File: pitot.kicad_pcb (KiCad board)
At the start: 2 copper layers, 15 parts, among them IC1 LT1167CN8PBF, IC2 LT1167CN8PBF, IC3 LT1167CN8PBF, IC4 LTC1144CN8#PBF, IC5 DEV-11114, P1 DIL8, P2 DIL8, P3 DIL8, P4 CONN_01X04, U1 LM7809CT

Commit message: size adj
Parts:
- moved P3 47.9 mm to (149.9, 53.3)
- moved P4 40.7 mm to (96.5, 96.5)
- moved P2 32.1 mm to (129.5, 53.3)
- moved IC5 30.5 mm to (109.2, 101.6)
- moved R3 28.1 mm to (157.5, 68.6)
- moved IC3 25.4 mm to (152.4, 68.6)
- moved P1 20.5 mm to (109.2, 53.3)
- moved R2 15.5 mm to (137.2, 68.6)
- moved IC2 12.7 mm to (132.1, 68.6)
- moved R1 3.59 mm to (116.8, 68.6)
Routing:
- net +5V: track 322.6 -> 170.2 mm
- net (no net): track 86.4 -> 0.00 mm
- net GND: track 457.0 -> 371.5 mm
- net Net-(IC5-Pad1): track 94.2 -> 33.9 mm
- net Net-(IC5-Pad2): track 87.9 -> 30.9 mm
- net Net-(IC3-Pad6): track 93.5 -> 40.6 mm
- net Net-(IC3-Pad2): track 44.5 -> 7.62 mm
- net Net-(IC3-Pad3): track 52.1 -> 15.2 mm
- net Net-(IC2-Pad6): track 55.6 -> 22.9 mm
- net Net-(IC2-Pad3): track 47.0 -> 15.2 mm
- net Net-(IC2-Pad2): track 39.4 -> 7.62 mm
- net Net-(IC1-Pad3): track 43.2 -> 15.2 mm
- net Net-(IC1-Pad2): track 35.6 -> 7.62 mm
- net Net-(C2-Pad2): track 101.9 -> 76.5 mm
- net Net-(IC1-Pad7): track 161.8 -> 136.4 mm
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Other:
- board outline added: 127 x 101.6 mm

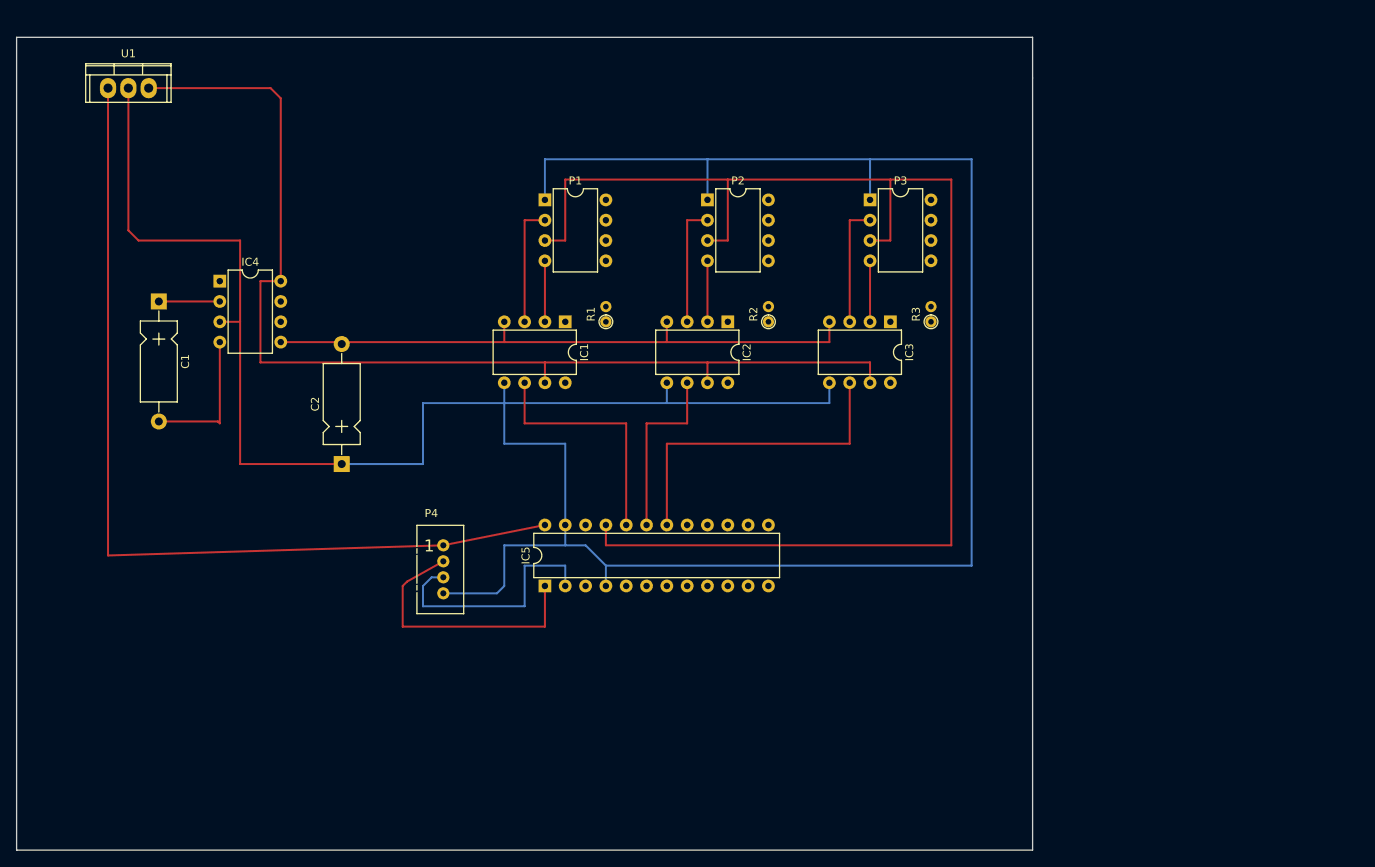
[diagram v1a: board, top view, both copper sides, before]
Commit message: add ZD and LPF
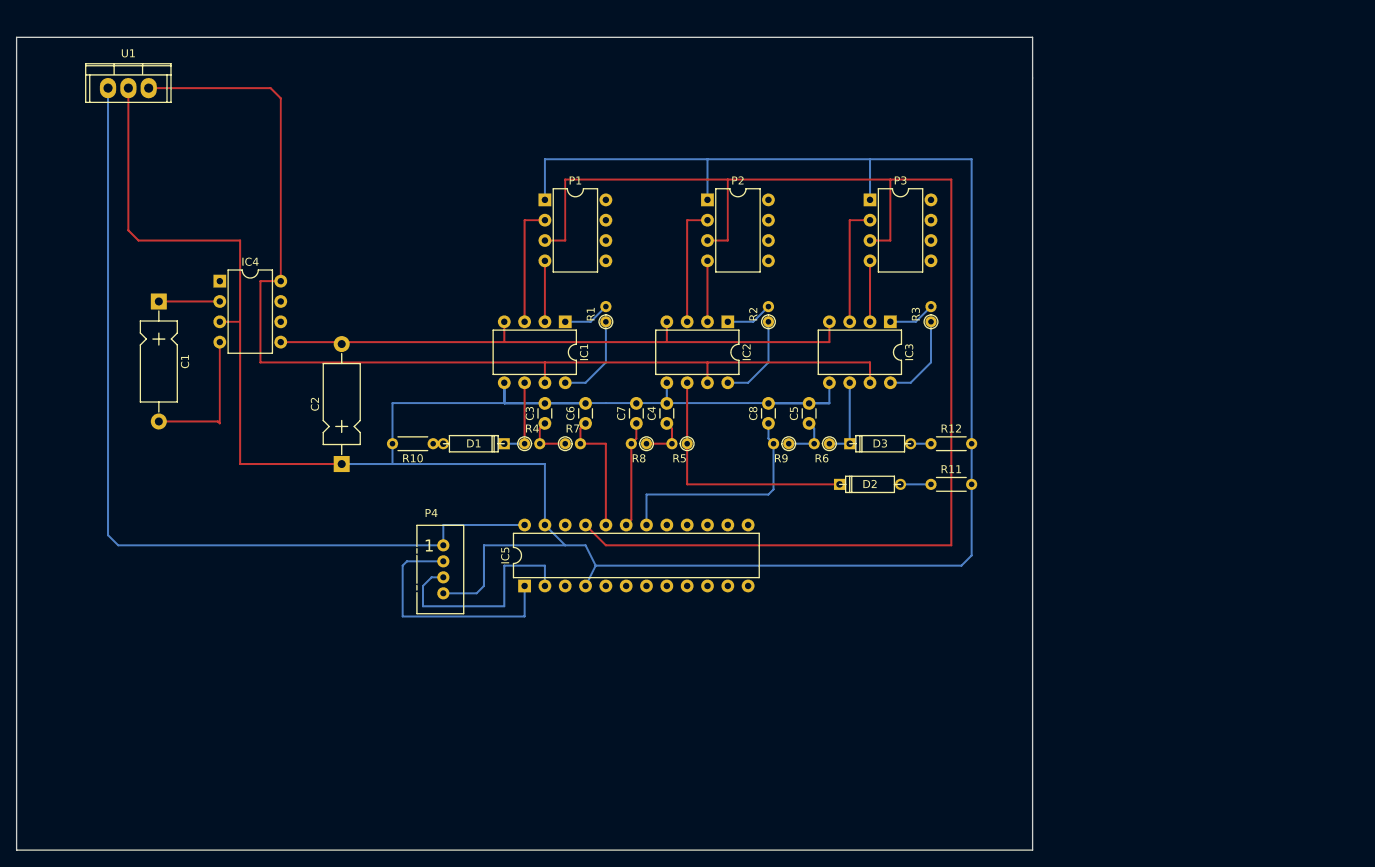
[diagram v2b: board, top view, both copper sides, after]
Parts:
- added C3: C, Capacitors_ThroughHole:C_Disc_D3.0mm_W1.6mm_P2.50mm, F.Cu at (109.2, 81.3)
- added C4: C, Capacitors_ThroughHole:C_Disc_D3.0mm_W1.6mm_P2.50mm, F.Cu at (124.5, 81.3)
- added C5: C, Capacitors_ThroughHole:C_Disc_D3.0mm_W1.6mm_P2.50mm, F.Cu at (142.2, 81.3)
- added C6: C, Capacitors_ThroughHole:C_Disc_D3.0mm_W1.6mm_P2.50mm, F.Cu at (114.3, 81.3)
- added C7: C, Capacitors_ThroughHole:C_Disc_D3.0mm_W1.6mm_P2.50mm, F.Cu at (120.7, 81.3)
- added C8: C, Capacitors_ThroughHole:C_Disc_D3.0mm_W1.6mm_P2.50mm, F.Cu at (137.2, 81.3)
- added D1: ZENER, Discret:D3, F.Cu at (100.3, 83.8)
- added D2: ZENER, Discret:D3, F.Cu at (149.9, 88.9)
- added D3: ZENER, Discret:D3, F.Cu at (151.1, 83.8)
- added R10: R, Resistors_ThroughHole:R_Axial_DIN0204_L3.6mm_D1.6mm_P5.08mm_Horizontal, F.Cu at (95.2, 83.8)
- added R11: R, Resistors_ThroughHole:R_Axial_DIN0204_L3.6mm_D1.6mm_P5.08mm_Horizontal, F.Cu at (157.5, 88.9)
- added R12: R, Resistors_ThroughHole:R_Axial_DIN0204_L3.6mm_D1.6mm_P5.08mm_Horizontal, F.Cu at (157.5, 83.8)
- added R4: R, Resistors_ThroughHole:R_Axial_DIN0204_L3.6mm_D1.6mm_P1.90mm_Vertical, F.Cu at (106.7, 83.8)
- added R5: R, Resistors_ThroughHole:R_Axial_DIN0204_L3.6mm_D1.6mm_P1.90mm_Vertical, F.Cu at (127.0, 83.8)
- added R6: R, Resistors_ThroughHole:R_Axial_DIN0204_L3.6mm_D1.6mm_P1.90mm_Vertical, F.Cu at (144.8, 83.8)
- added R7: R, Resistors_ThroughHole:R_Axial_DIN0204_L3.6mm_D1.6mm_P1.90mm_Vertical, F.Cu at (111.8, 83.8)
- added R8: R, Resistors_ThroughHole:R_Axial_DIN0204_L3.6mm_D1.6mm_P1.90mm_Vertical, F.Cu at (121.9, 83.8)
- added R9: R, Resistors_ThroughHole:R_Axial_DIN0204_L3.6mm_D1.6mm_P1.90mm_Vertical, F.Cu at (139.7, 83.8)
- moved IC5 2.54 mm to (106.7, 101.6)
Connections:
- IC1 pad 6: Net-(IC1-Pad6) -> Net-(D1-Pad1)
- IC2 pad 6: Net-(IC2-Pad6) -> Net-(D2-Pad1)
- IC3 pad 6: Net-(IC3-Pad6) -> Net-(D3-Pad1)
- IC5 pad 18: Net-(IC3-Pad6) -> Net-(C8-Pad1)
- IC5 pad 19: Net-(IC2-Pad6) -> Net-(C7-Pad1)
- IC5 pad 20: Net-(IC1-Pad6) -> Net-(C6-Pad1)
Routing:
- net Net-(IC3-Pad6): track 40.6 -> 0.00 mm
- net Net-(D2-Pad1): track 0.00 -> 31.8 mm
- net Net-(IC1-Pad6): track 30.5 -> 0.00 mm
- net Net-(C8-Pad1): track 0.00 -> 28.5 mm
- net GND: track 371.5 -> 399.5 mm
- net Net-(IC2-Pad6): track 22.9 -> 0.00 mm
- net Net-(C6-Pad1): track 0.00 -> 16.1 mm
- net Net-(C7-Pad1): track 0.00 -> 13.2 mm
- net Net-(IC1-Pad8): track 0.00 -> 11.2 mm
- net Net-(IC3-Pad8): track 0.00 -> 11.2 mm
- net Net-(IC2-Pad8): track 0.00 -> 11.2 mm
- net Net-(D1-Pad1): track 0.00 -> 10.2 mm
- net Net-(D3-Pad1): track 0.00 -> 10.2 mm
- net Net-(C3-Pad1): track 0.00 -> 5.99 mm
- net Net-(C5-Pad1): track 0.00 -> 5.99 mm
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
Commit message: mod pcb layout
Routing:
- net GND: track 399.5 -> 400.9 mm
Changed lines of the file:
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@@
     (links 70)
     (no_connects 2)
-    (area 31.925717 27.63 175.997143 134.695001)
+    (area 43.104999 32.944999 170.255001 134.695001)
     (thickness 1.6)
     (drawings 13)
-    (tracks 161)
+    (tracks 160)
     (zones 0)
     (modules 33)
@@
     (pad_to_mask_clearance 0.2)
     (aux_axis_origin 0 0)
-    (grid_origin 83.82 104.14)
     (visible_elements 7FFFFFFF)
     (pcbplotparams
@@
   (gr_line (start 43.18 134.62) (end 170.18 134.62) (angle 90) (layer Edge.Cuts) (width 0.15))
   (gr_line (start 43.18 33.02) (end 43.18 134.62) (angle 90) (layer Edge.Cuts) (width 0.15))
-  (segment (start 96.52 102.52) (end 100.68 102.52) (width 0.25) (layer B.Cu) (net 1) (status 400000))
-  (segment (start 101.6 96.52) (end 111.76 96.52) (width 0.25) (layer B.Cu) (net 1))
-  (segment (start 101.6 101.6) (end 101.6 96.52) (width 0.25) (layer B.Cu) (net 1))
-  (segment (start 100.68 102.52) (end 101.6 101.6) (width 0.25) (layer B.Cu) (net 1))
-  (segment (start 162.56 88.9) (end 162.56 97.79) (width 0.25) (layer B.Cu) (net 1))
-  (segment (start 161.29 99.06) (end 115.57 99.06) (width 0.25) (layer B.Cu) (net 1))
-  (segment (start 162.56 97.79) (end 161.29 99.06) (width 0.25) (layer B.Cu) (net 1))
+  (segment (start 83.82 86.36) (end 83.82 88.9) (width 0.25) (layer B.Cu) (net 1))
+  (segment (start 88.9 88.9) (end 83.82 88.9) (width 0.25) (layer B.Cu) (net 1))
+  (segment (start 88.9 88.9) (end 90.17 88.9) (width 0.25) (layer B.Cu) (net 1))
+  (segment (start 109.22 93.98) (end 109.22 96.52) (width 0.25) (layer B.Cu) (net 1))
+  (segment (start 114.3 99.06) (end 111.76 96.52) (width 0.25) (layer B.Cu) (net 1))
+  (segment (start 111.76 96.52) (end 109.22 96.52) (width 0.25) (layer B.Cu) (net 1))
+  (segment (start 100.68 102.52) (end 96.52 102.52) (width 0.25) (layer B.Cu) (net 1))
+  (segment (start 109.22 96.52) (end 101.6 96.52) (width 0.25) (layer B.Cu) (net 1))
+  (segment (start 101.6 96.52) (end 101.6 101.6) (width 0.25) (layer B.Cu) (net 1))
+  (segment (start 101.6 101.6) (end 100.68 102.52) (width 0.25) (layer B.Cu) (net 1))
+  (segment (start 114.3 101.6) (end 114.3 99.06) (width 0.25) (layer B.Cu) (net 1))
+  (segment (start 162.56 99.06) (end 162.56 88.9) (width 0.25) (layer B.Cu) (net 1))
+  (segment (start 114.3 99.06) (end 162.56 99.06) (width 0.25) (layer B.Cu) (net 1))
   (segment (start 162.56 83.82) (end 162.56 88.9) (width 0.25) (layer B.Cu) (net 1))
-  (segment (start 90.17 86.36) (end 109.22 86.36) (width 0.25) (layer B.Cu) (net 1))
-  (segment (start 109.22 86.36) (end 109.22 93.98) (width 0.25) (layer B.Cu) (net 1))
-  (segment (start 90.17 83.82) (end 90.17 86.36) (width 0.25) (layer B.Cu) (net 1))
+  (segment (start 90.17 88.9) (end 109.22 88.9) (width 0.25) (layer B.Cu) (net 1))
+  (segment (start 109.22 88.9) (end 109.22 93.98) (width 0.25) (layer B.Cu) (net 1))
+  (segment (start 90.17 83.82) (end 90.17 88.9) (width 0.25) (layer B.Cu) (net 1) (status 10))
   (segment (start 104.14 78.74) (end 90.17 78.74) (width 0.25) (layer B.Cu) (net 1))
-  (segment (start 90.17 78.74) (end 90.17 83.82) (width 0.25) (layer B.Cu) (net 1))
-  (segment (start 88.9 86.36) (end 90.17 86.36) (width 0.25) (layer B.Cu) (net 1))
-  (segment (start 88.9 86.36) (end 83.82 86.36) (width 0.25) (layer B.Cu) (net 1))
-  (segment (start 114.3 78.78) (end 104.18 78.78) (width 0.25) (layer B.Cu) (net 1))
+  (segment (start 90.17 78.74) (end 90.17 83.82) (width 0.25) (layer B.Cu) (net 1) (status 20))
+  (segment (start 114.3 78.78) (end 104.18 78.78) (width 0.25) (layer B.Cu) (net 1) (status 10))
   (segment (start 104.18 78.78) (end 104.14 78.74) (width 0.25) (layer B.Cu) (net 1))
   (segment (start 104.14 78.74) (end 104.14 76.2) (width 0.25) (layer B.Cu) (net 1))
@@
   (segment (start 142.24 78.78) (end 144.74 78.78) (width 0.25) (layer B.Cu) (net 1))
   (segment (start 144.74 78.78) (end 144.78 78.74) (width 0.25) (layer B.Cu) (net 1))
-  (segment (start 114.3 101.6) (end 115.57 99.06) (width 0.25) (layer B.Cu) (net 1) (status 10))
-  (segment (start 115.57 99.06) (end 114.3 96.52) (width 0.25) (layer B.Cu) (net 1))
-  (segment (start 114.3 96.52) (end 111.76 96.52) (width 0.25) (layer B.Cu) (net 1))
-  (segment (start 111.76 96.52) (end 109.22 93.98) (width 0.25) (layer B.Cu) (net 1) (status 20))
-  (segment (start 115.57 99.06) (end 115.57 99.06) (width 0.25) (layer B.Cu) (net 1) (status 20))
   (segment (start 109.22 53.34) (end 109.22 48.26) (width 0.25) (layer B.Cu) (net 1))
   (segment (start 129.54 53.34) (end 129.54 48.26) (width 0.25) (layer B.Cu) (net 1))
@@
   (segment (start 132.08 50.8) (end 152.4 50.8) (width 0.25) (layer F.Cu) (net 2))
   (segment (start 111.76 58.42) (end 111.76 50.8) (width 0.25) (layer F.Cu) (net 2))
-  (segment (start 96.52 96.52) (end 55.88 96.52) (width 0.25) (layer B.Cu) (net 3) (status 400000))
-  (segment (start 54.61 95.25) (end 54.61 39.37) (width 0.25) (layer B.Cu) (net 3) (status 800000))
+  (segment (start 96.52 96.52) (end 55.88 96.52) (width 0.25) (layer B.Cu) (net 3))
+  (segment (start 54.61 95.25) (end 54.61 39.37) (width 0.25) (layer B.Cu) (net 3))
   (segment (start 55.88 96.52) (end 54.61 95.25) (width 0.25) (layer B.Cu) (net 3))
-  (segment (start 106.68 93.98) (end 96.52 93.98) (width 0.25) (layer B.Cu) (net 3) (status 400000))
-  (segment (start 96.52 93.98) (end 96.52 96.52) (width 0.25) (layer B.Cu) (net 3) (status 800000))
+  (segment (start 106.68 93.98) (end 96.52 93.98) (width 0.25) (layer B.Cu) (net 3))
+  (segment (start 96.52 93.98) (end 96.52 96.52) (width 0.25) (layer B.Cu) (net 3))
   (segment (start 68.58 66.04) (end 60.96 66.04) (width 0.25) (layer F.Cu) (net 4))
   (segment (start 68.58 71.12) (end 68.58 81.28) (width 0.25) (layer F.Cu) (net 5))
@@
   (segment (start 91.44 105.41) (end 91.44 99.06) (width 0.25) (layer B.Cu) (net 20))
   (segment (start 106.68 105.41) (end 91.44 105.41) (width 0.25) (layer B.Cu) (net 20))
-  (segment (start 96.52 100.52) (end 95.06 100.52) (width 0.25) (layer B.Cu) (net 21) (status 400000))
-  (segment (start 109.22 99.06) (end 109.22 101.6) (width 0.25) (layer B.Cu) (net 21) (status 800000))
+  (segment (start 109.22 101.6) (end 109.22 101.6) (width 0.25) (layer F.Cu) (net 21) (status 30))
+  (segment (start 96.52 100.52) (end 95.06 100.52) (width 0.25) (layer B.Cu) (net 21))
+  (segment (start 109.22 99.06) (end 109.22 101.6) (width 0.25) (layer B.Cu) (net 21))
   (segment (start 104.14 99.06) (end 109.22 99.06) (width 0.25) (layer B.Cu) (net 21))
   (segment (start 104.14 104.14) (end 104.14 99.06) (width 0.25) (layer B.Cu) (net 21))
@@
   (segment (start 93.98 101.6) (end 93.98 104.14) (width 0.25) (layer B.Cu) (net 21))
   (segment (start 95.06 100.52) (end 93.98 101.6) (width 0.25) (layer B.Cu) (net 21))
-  (segment (start 109.22 101.6) (end 109.22 101.6) (width 0.25) (layer F.Cu) (net 21) (status 30))
-  (segment (start 108.58 83.82) (end 108.58 81.92) (width 0.25) (layer F.Cu) (net 22))
+  (segment (start 108.58 83.82) (end 108.58 81.92) (width 0.25) (layer F.Cu) (net 22) (status 10))
   (segment (start 108.58 81.92) (end 109.22 81.28) (width 0.25) (layer F.Cu) (net 22) (status 20))
-  (segment (start 108.58 83.82) (end 111.76 83.82) (width 0.25) (layer F.Cu) (net 22))
+  (segment (start 108.58 83.82) (end 111.76 83.82) (width 0.25) (layer F.Cu) (net 22) (status 20))
   (segment (start 125.1 83.82) (end 121.92 83.82) (width 0.25) (layer F.Cu) (net 23))
   (segment (start 125.1 83.82) (end 125.1 81.92) (width 0.25) (layer F.Cu) (net 23))
@@
   (segment (start 142.88 83.82) (end 142.88 81.92) (width 0.25) (layer B.Cu) (net 24))
   (segment (start 142.88 81.92) (end 142.24 81.28) (width 0.25) (layer B.Cu) (net 24))
-  (segment (start 113.66 83.82) (end 116.84 83.82) (width 0.25) (layer F.Cu) (net 25))
+  (segment (start 113.66 83.82) (end 116.84 83.82) (width 0.25) (layer F.Cu) (net 25) (status 10))
   (segment (start 116.84 83.82) (end 116.84 93.98) (width 0.25) (layer F.Cu) (net 25))
-  (segment (start 113.66 83.82) (end 113.66 81.92) (width 0.25) (layer F.Cu) (net 25))
-  (segment (start 113.66 81.92) (end 114.3 81.28) (width 0.25) (layer F.Cu) (net 25))
+  (segment (start 113.66 83.82) (end 113.66 81.92) (width 0.25) (layer F.Cu) (net 25) (status 10))
+  (segment (start 113.66 81.92) (end 114.3 81.28) (width 0.25) (layer F.Cu) (net 25) (status 20))
   (segment (start 120.02 83.82) (end 120.02 93.34) (width 0.25) (layer F.Cu) (net 26))
   (segment (start 120.02 93.34) (end 119.38 93.98) (width 0.25) (layer F.Cu) (net 26))
@@
   (segment (start 137.16 81.28) (end 137.16 83.18) (width 0.25) (layer B.Cu) (net 27))
   (segment (start 137.16 83.18) (end 137.8 83.82) (width 0.25) (layer B.Cu) (net 27))
-  (segment (start 95.25 83.82) (end 96.52 83.82) (width 0.25) (layer B.Cu) (net 28) (status 10))
+  (segment (start 95.25 83.82) (end 96.52 83.82) (width 0.25) (layer B.Cu) (net 28) (status 20))
   (segment (start 153.67 88.9) (end 157.48 88.9) (width 0.25) (layer B.Cu) (net 29) (status 10))
   (segment (start 154.94 83.82) (end 157.48 83.82) (width 0.25) (layer B.Cu) (net 30) (status 20))
-  (segment (start 104.14 83.82) (end 106.68 83.82) (width 0.25) (layer B.Cu) (net 31) (status C00000))
-  (segment (start 106.68 76.2) (end 106.68 83.82) (width 0.25) (layer F.Cu) (net 31))
+  (segment (start 104.14 83.82) (end 106.68 83.82) (width 0.25) (layer B.Cu) (net 31) (status 20))
+  (segment (start 106.68 76.2) (end 106.68 83.82) (width 0.25) (layer F.Cu) (net 31) (status 20))
   (segment (start 146.05 88.9) (end 127 88.9) (width 0.25) (layer F.Cu) (net 32))
   (segment (start 127 88.9) (end 127 83.82) (width 0.25) (layer F.Cu) (net 32))
